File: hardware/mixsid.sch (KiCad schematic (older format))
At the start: 63 parts, among them P1 INPUT, P2 CONTROL, P4 SOCKET LEFT, P5 OUTPUT, P6 SOCKET RIGHT, Q1 BC547, Q2 BC547, U1 GAL16V8, U2 SID2, U3 7812, U4 7809, U5 SID1, U6 4052, U8 ICL7660

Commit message: Project renamed to MixSID
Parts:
- U1: symbol SMARTSID -> MIXSID
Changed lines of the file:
@@
 LIBS:valves
 LIBS:mos6581
-LIBS:smartsid
+LIBS:mixsid
 LIBS:lm78xx
 LIBS:7660
-LIBS:smartsid-cache
+LIBS:mixsid-cache
 EELAYER 25 0
 EELAYER END
@@
 encoding utf-8
 Sheet 1 1
-Title "SmartSID - C64 stereo SID addon board"
+Title "MixSID - C64 stereo SID addon board"
 Date "2016-03-09"
 Rev "1"
 Comp "Henning Bekel"
-Comment1 "www.henning-bekel.de/smartsid"
+Comment1 ""
 Comment2 ""
 Comment3 ""
@@
 $EndComp
 $Comp
-L SMARTSID U1
+L MIXSID U1
 U 1 1 56D81BBF
 P 9300 3450

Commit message: Hardware: Improved routing, placement of 7812 and caps, silkscreen
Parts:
- U3, U4: footprint Power_Integrations:TO-220 -> Pinheaders:TO-220
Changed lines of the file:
@@
 F 0 "U3" H 3550 6804 60  0000 C CNN
 F 1 "7812" H 3400 7200 60  0000 C CNN
-F 2 "Power_Integrations:TO-220" H 3400 7000 60  0001 C CNN
+F 2 "Pinheaders:TO-220" H 3400 7000 60  0001 C CNN
 F 3 "" H 3400 7000 60  0000 C CNN
 	1    3400 7000
@@
 F 0 "U4" H 5300 6804 60  0000 C CNN
 F 1 "7809" H 5150 7200 60  0000 C CNN
-F 2 "Power_Integrations:TO-220" H 5150 7000 60  0001 C CNN
+F 2 "Pinheaders:TO-220" H 5150 7000 60  0001 C CNN
 F 3 "" H 5150 7000 60  0000 C CNN
 	1    5150 7000

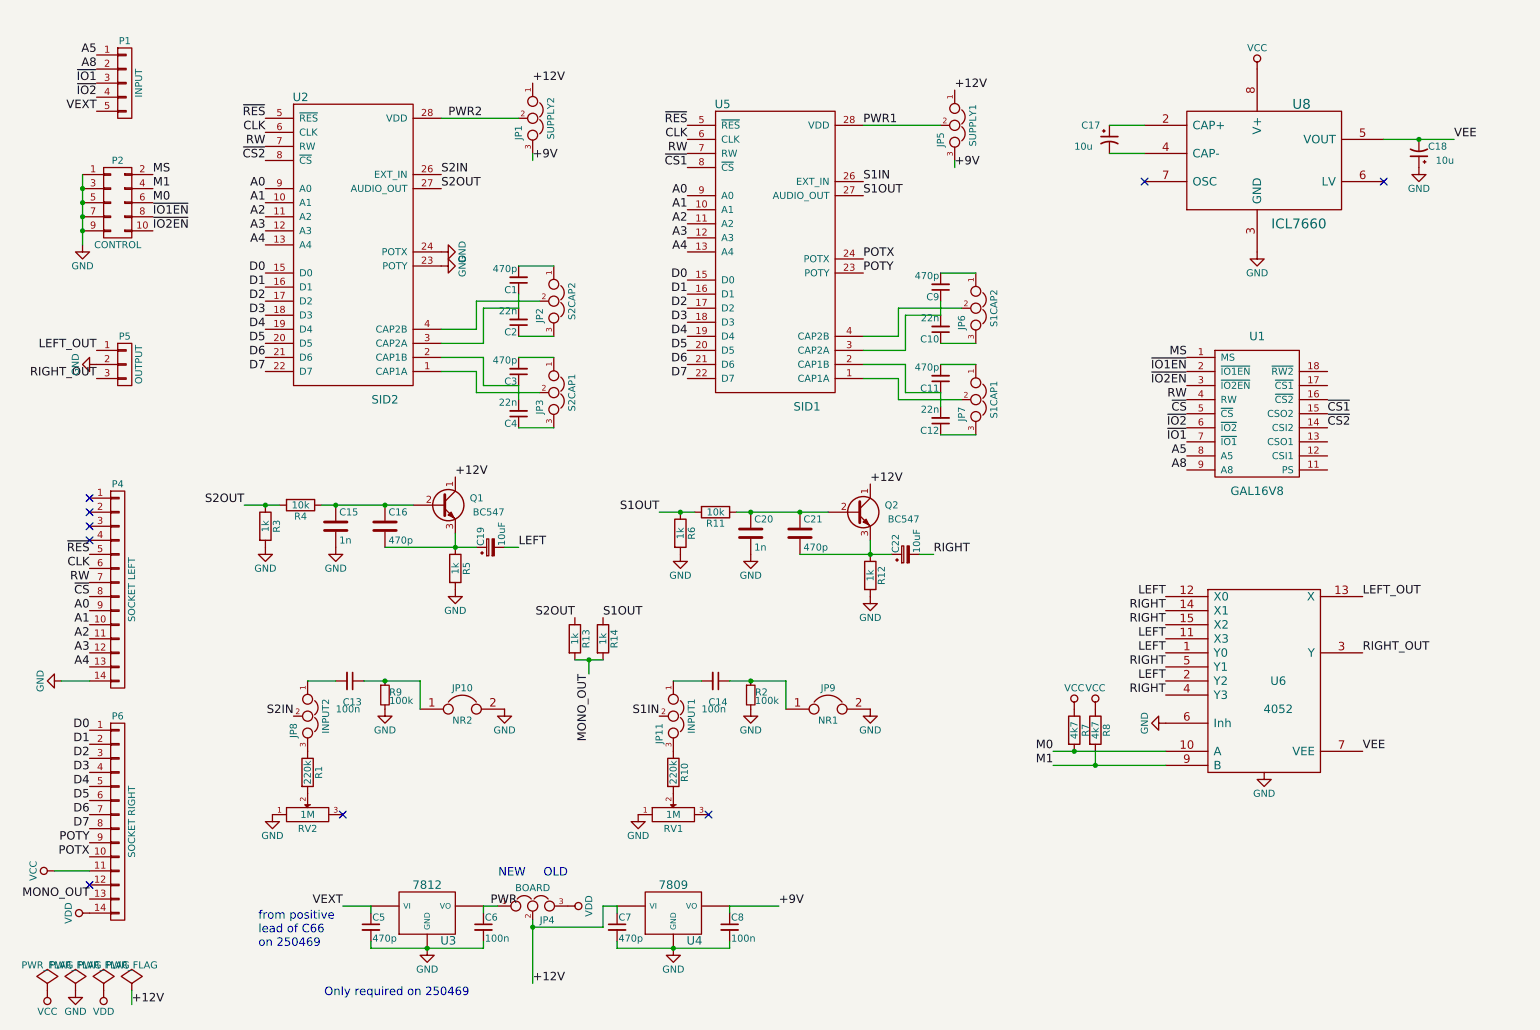
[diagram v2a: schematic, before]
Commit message: Hardware: Added voltage dividers for optional volume adjustments
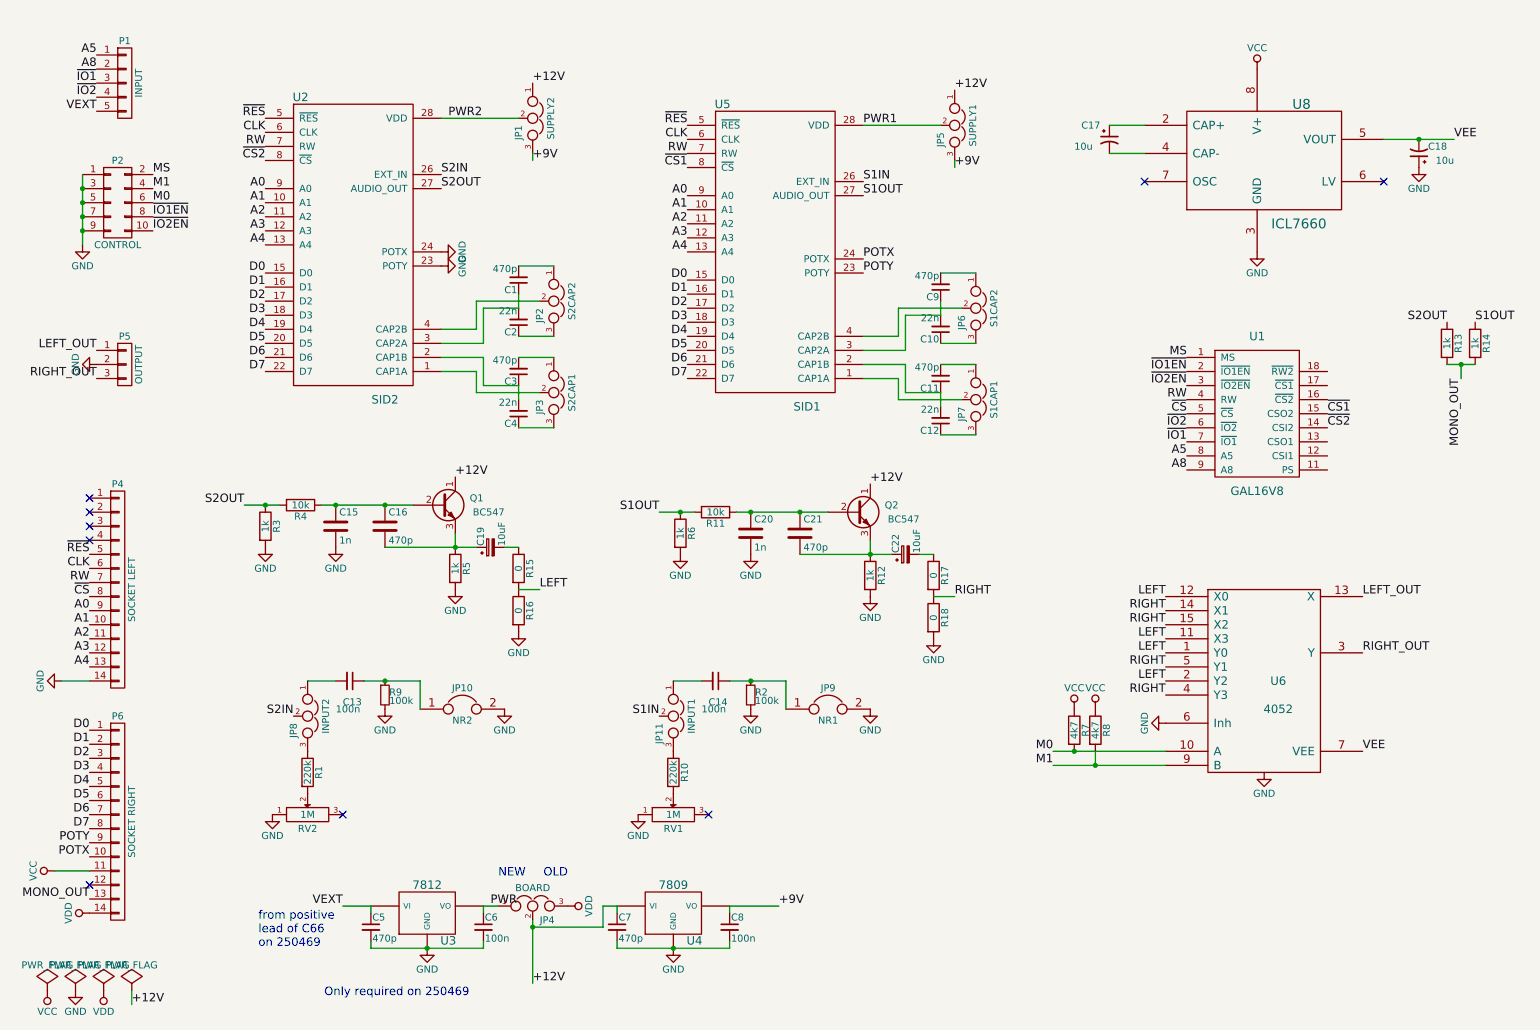
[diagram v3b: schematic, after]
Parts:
- added R15, R16, R17, R18: 0, Discret:R1, symbol R
- C19, C22: footprint Capacitors_ThroughHole:C_Radial_D5_L6_P2.5 -> Pinheaders:C_Radial_D5_L6_P2.5
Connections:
- net GND: now also R16.2, R18.2
- net LEFT: now also R15.2, R16.1; no longer C19.2
- net RIGHT: now also R17.2, R18.1; no longer C22.2
- new net: C19.2, R15.1
- new net: C22.2, R17.1
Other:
- moved on the sheet: R13, R14
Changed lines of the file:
@@
 	0    1    1    0
 $EndComp
-Text Label 7000 4450 0    60   ~ 0
+Text Label 7150 4750 0    60   ~ 0
 RIGHT
-Text Label 4050 4400 0    60   ~ 0
+Text Label 4200 4700 0    60   ~ 0
 LEFT
 $Comp
@@
 Connection ~ 950  2050
 Connection ~ 950  2150
-Text Label 4450 4900 2    60   ~ 0
+Text Label 10650 2800 2    60   ~ 0
 S2OUT
-Text Label 4650 4900 0    60   ~ 0
+Text Label 10850 2800 0    60   ~ 0
 S1OUT
 $Comp
 L R R13
 U 1 1 56EC71A3
-P 4450 5050
-F 0 "R13" V 4530 5050 50  0000 C CNN
-F 1 "1k" V 4450 5050 50  0000 C CNN
-F 2 "Discret:R1" V 4380 5050 50  0001 C CNN
-F 3 "" H 4450 5050 50  0000 C CNN
-	1    4450 5050
+P 10650 2950
+F 0 "R13" V 10730 2950 50  0000 C CNN
+F 1 "1k" V 10650 2950 50  0000 C CNN
+F 2 "Discret:R1" V 10580 2950 50  0001 C CNN
+F 3 "" H 10650 2950 50  0000 C CNN
+	1    10650 2950
 	1    0    0    -1
 $EndComp
@@
 L R R14
 U 1 1 56EC7384
-P 4650 5050
-F 0 "R14" V 4730 5050 50  0000 C CNN
-F 1 "1k" V 4650 5050 50  0000 C CNN
-F 2 "Discret:R1" V 4580 5050 50  0001 C CNN
-F 3 "" H 4650 5050 50  0000 C CNN
-	1    4650 5050
-	1    0    0    -1
-$EndComp
-Wire Wire Line
-	4450 5200 4650 5200
-Wire Wire Line
-	4550 5200 4550 5300
-Connection ~ 4550 5200
-Text Label 4550 5300 3    60   ~ 0
+P 10850 2950
+F 0 "R14" V 10930 2950 50  0000 C CNN
+F 1 "1k" V 10850 2950 50  0000 C CNN
+F 2 "Discret:R1" V 10780 2950 50  0001 C CNN
+F 3 "" H 10850 2950 50  0000 C CNN
+	1    10850 2950
+	1    0    0    -1
+$EndComp
+Wire Wire Line
+	10650 3100 10850 3100
+Wire Wire Line
+	10750 3100 10750 3200
+Connection ~ 10750 3100
+Text Label 10750 3200 3    60   ~ 0
 MONO_OUT
 Text Label 1000 6900 2    60   ~ 0
@@
 F 0 "C19" H 3860 4470 50  0000 L CNN
 F 1 "10uF" H 3860 4320 50  0000 L CNN
-F 2 "Capacitors_ThroughHole:C_Radial_D5_L6_P2.5" H 3850 4400 60  0001 C CNN
+F 2 "Pinheaders:C_Radial_D5_L6_P2.5" H 3850 4400 60  0001 C CNN
 F 3 "" H 3850 4400 60  0000 C CNN
 	1    3850 4400
@@
 F 0 "C22" H 6810 4520 50  0000 L CNN
 F 1 "10uF" H 6810 4370 50  0000 L CNN
-F 2 "Capacitors_ThroughHole:C_Radial_D5_L6_P2.5" H 6800 4450 60  0001 C CNN
+F 2 "Pinheaders:C_Radial_D5_L6_P2.5" H 6800 4450 60  0001 C CNN
 F 3 "" H 6800 4450 60  0000 C CNN
 	1    6800 4450
@@
 	1    0    0    -1
 $EndComp
+$Comp
+L R R15
+U 1 1 571F33A7
+P 4050 4550
+F 0 "R15" V 4130 4550 50  0000 C CNN
+F 1 "0" V 4050 4550 50  0000 C CNN
+F 2 "Discret:R1" V 3980 4550 30  0001 C CNN
+F 3 "" H 4050 4550 30  0000 C CNN
+	1    4050 4550
+	1    0    0    -1
+$EndComp
+$Comp
+L R R16
+U 1 1 571F3464
+P 4050 4850
+F 0 "R16" V 4130 4850 50  0000 C CNN
+F 1 "0" V 4050 4850 50  0000 C CNN
+F 2 "Discret:R1" V 3980 4850 30  0001 C CNN
+F 3 "" H 4050 4850 30  0000 C CNN
+	1    4050 4850
+	1    0    0    -1
+$EndComp
+Wire Wire Line
+	4050 4700 4200 4700
+$Comp
+L GND #PWR037
+U 1 1 571F3E41
+P 4050 5000
+F 0 "#PWR037" H 4050 4750 50  0001 C CNN
+F 1 "GND" H 4050 4850 50  0000 C CNN
+F 2 "" H 4050 5000 60  0000 C CNN
+F 3 "" H 4050 5000 60  0000 C CNN
+	1    4050 5000
+	1    0    0    -1
+$EndComp
+$Comp
+L R R17
+U 1 1 571F4403
+P 7000 4600
+F 0 "R17" V 7080 4600 50  0000 C CNN
+F 1 "0" V 7000 4600 50  0000 C CNN
+F 2 "Discret:R1" V 6930 4600 30  0001 C CNN
+F 3 "" H 7000 4600 30  0000 C CNN
+	1    7000 4600
+	1    0    0    -1
+$EndComp
+$Comp
+L R R18
+U 1 1 571F4409
+P 7000 4900
+F 0 "R18" V 7080 4900 50  0000 C CNN
+F 1 "0" V 7000 4900 50  0000 C CNN
+F 2 "Discret:R1" V 6930 4900 30  0001 C CNN
+F 3 "" H 7000 4900 30  0000 C CNN
+	1    7000 4900
+	1    0    0    -1
+$EndComp
+Wire Wire Line
+	7000 4750 7150 4750
+$Comp
+L GND #PWR038
+U 1 1 571F4410
+P 7000 5050
+F 0 "#PWR038" H 7000 4800 50  0001 C CNN
+F 1 "GND" H 7000 4900 50  0000 C CNN
+F 2 "" H 7000 5050 60  0000 C CNN
+F 3 "" H 7000 5050 60  0000 C CNN
+	1    7000 5050
+	1    0    0    -1
+$EndComp

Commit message: Hardware: Changed 7660 caps to small electrolytics, improved silkscreen
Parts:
- C17, C18: footprint Capacitors_ThroughHole:C_Disc_D3_P2.5 -> Pinheaders:C_Radial_D5_L6_P2.5
- R16, R18: value 0 -> ∞
- U8: footprint Housings_DIP:DIP-8_W7.62mm -> Pinheaders:DIP-8_W7.62mm
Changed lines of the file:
@@
 F 0 "U8" H 9550 2050 70  0000 L CNN
 F 1 "ICL7660" H 9400 1200 70  0000 L CNN
-F 2 "Housings_DIP:DIP-8_W7.62mm" H 9350 1650 60  0001 C CNN
+F 2 "Pinheaders:DIP-8_W7.62mm" H 9350 1650 60  0001 C CNN
 F 3 "" H 9350 1650 60  0000 C CNN
 	1    9350 1650
@@
 F 0 "C17" H 8050 1600 50  0000 L CNN
 F 1 "10u" H 8000 1450 50  0000 L CNN
-F 2 "Capacitors_ThroughHole:C_Disc_D3_P2.5" H 8250 1500 60  0001 C CNN
+F 2 "Pinheaders:C_Radial_D5_L6_P2.5" H 8250 1500 60  0001 C CNN
 F 3 "" H 8250 1500 60  0000 C CNN
 	1    8250 1500
@@
 F 0 "C18" H 10250 1550 50  0000 L CNN
 F 1 "10u" H 10200 1650 50  0000 L CNN
-F 2 "Capacitors_ThroughHole:C_Disc_D3_P2.5" H 10450 1600 60  0001 C CNN
+F 2 "Pinheaders:C_Radial_D5_L6_P2.5" H 10450 1600 60  0001 C CNN
 F 3 "" H 10450 1600 60  0000 C CNN
 	1    10450 1600
@@
 P 4050 4850
 F 0 "R16" V 4130 4850 50  0000 C CNN
-F 1 "0" V 4050 4850 50  0000 C CNN
+F 1 "∞" V 4050 4850 50  0000 C CNN
 F 2 "Discret:R1" V 3980 4850 30  0001 C CNN
 F 3 "" H 4050 4850 30  0000 C CNN
@@
 P 7000 4900
 F 0 "R18" V 7080 4900 50  0000 C CNN
-F 1 "0" V 7000 4900 50  0000 C CNN
+F 1 "∞" V 7000 4900 50  0000 C CNN
 F 2 "Discret:R1" V 6930 4900 30  0001 C CNN
 F 3 "" H 7000 4900 30  0000 C CNN

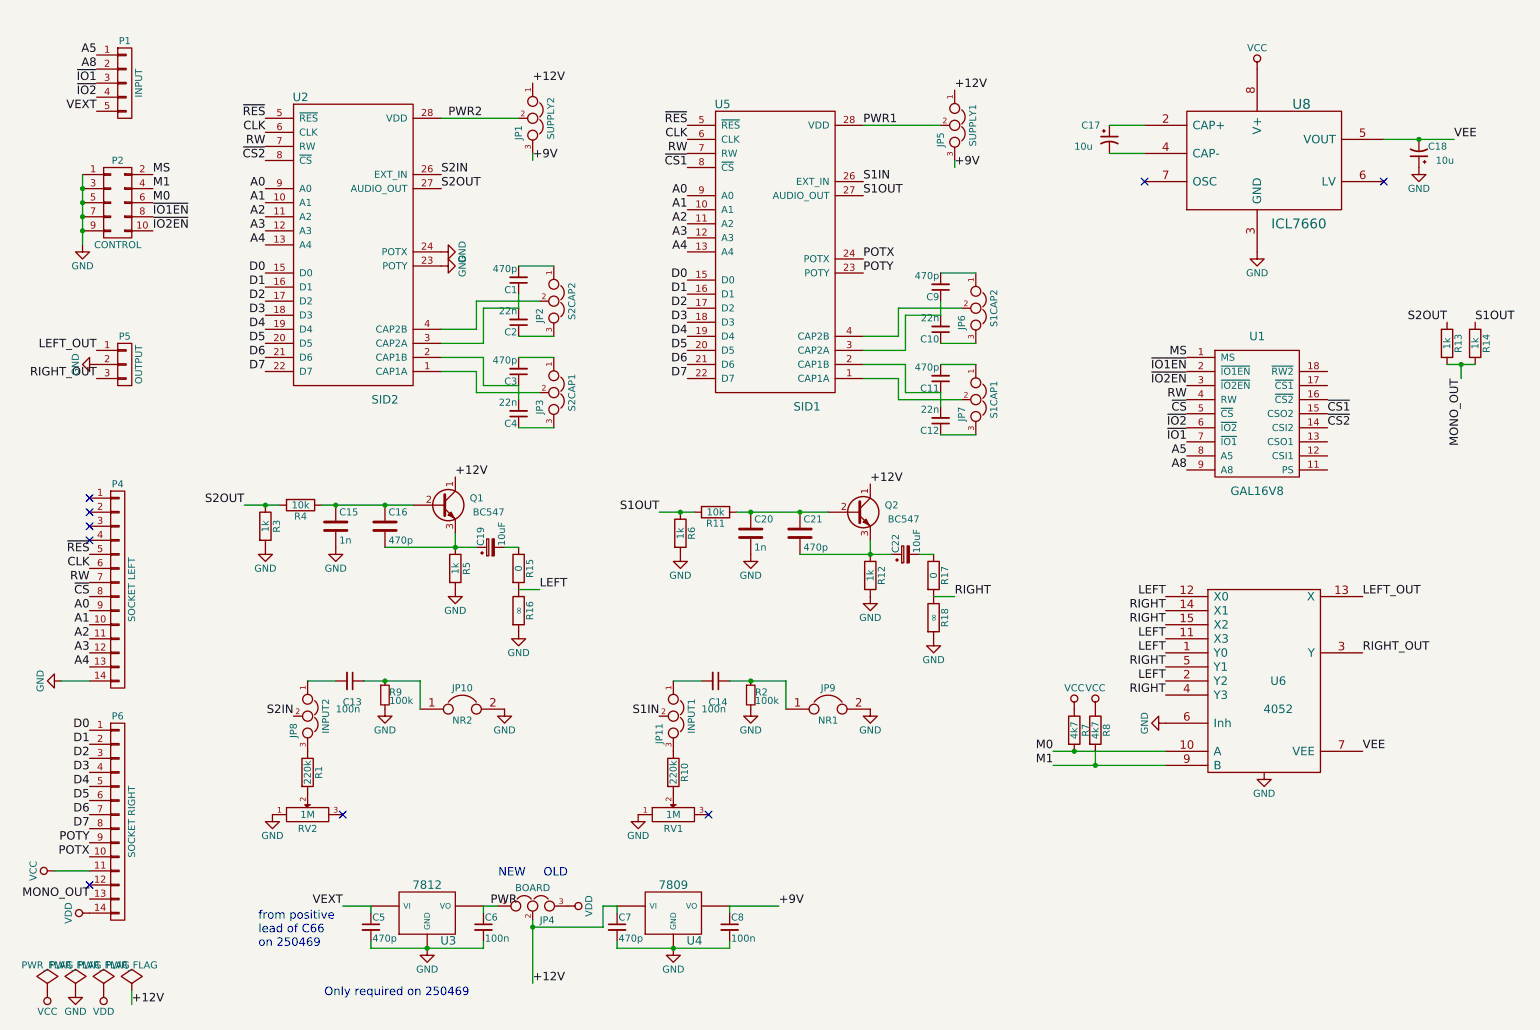
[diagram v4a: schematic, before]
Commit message: Hardware: Priority, paddle multiplexing, volume adjust, bigger board size
Priority select has been reimplemented, allowing to virtually swap sids in
terms of addressing (which SID stays at home and which one goes stereo).

A 4053 multiplexer has been added to keep the paddles working regardless of
priority. Paddle lines are always routed to the SID currently at $d400.

Two pots have been added to allow volume adjustments before mixing in order
to adjust two different models in overall volume (6581 are usually louder).
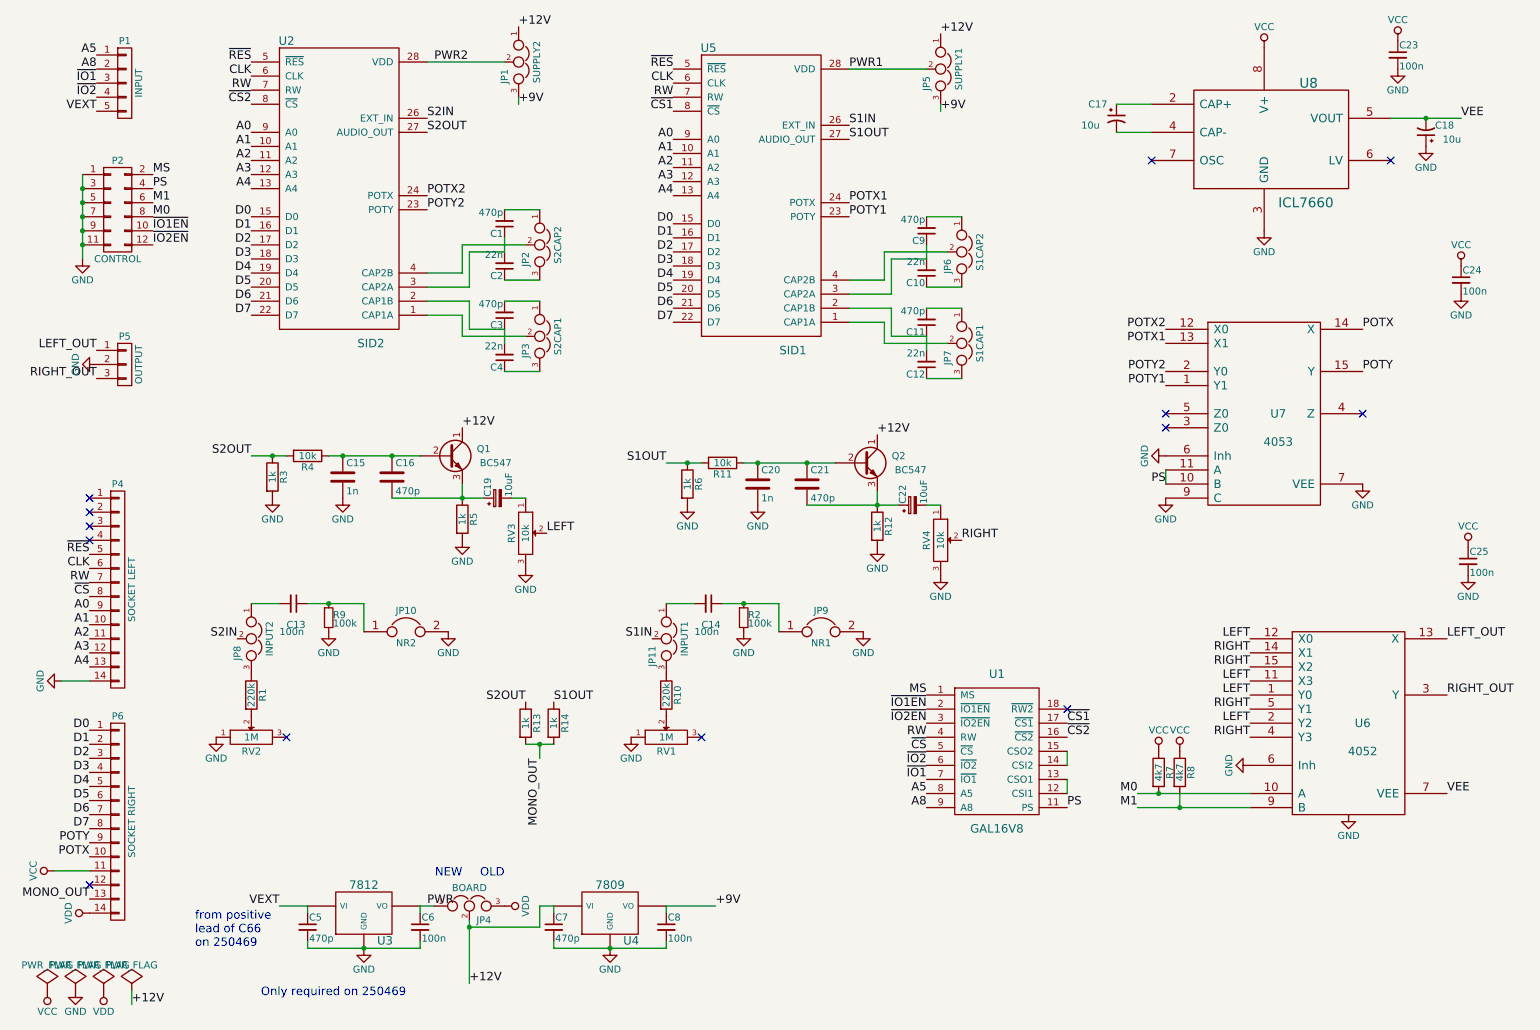
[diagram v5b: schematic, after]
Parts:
- removed P2: CONTROL, Pinheaders:Pin_Header_Straight_2x05, symbol CONN_02X05
- removed R15, R17: 0, Discret:R1, symbol R
- removed R16, R18: ∞, Discret:R1, symbol R
- added C23, C24, C25: 100n, Capacitors_ThroughHole:C_Disc_D3_P2.5, symbol C_Small
- added P2: CONTROL, Pinheaders:Pin_Header_Straight_2x06, symbol CONN_02X06
- added RV3, RV4: 10k, Potentiometers:Potentiometer_Bourns_3296W_3-8Zoll_Inline_ScrewUp, symbol POT
- added U7: 4053, Housings_DIP:DIP-16_W7.62mm, symbol 4053
- R7, R8: footprint Discret:R3 -> Discret:R1
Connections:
- net GND: now also C23.2, C24.2, C25.2, P2.1 (P1), P2.11 (P11), P2.3 (P3), P2.5 (P5), P2.7 (P7), P2.9 (P9), RV3.3, RV4.3, U7.6 (Inh), U7.7 (VEE), U7.8 (GND), U7.9 (C); no longer U2.23 (POTY), U2.24 (POTX)
- net LEFT: now also RV3.2
- net M0: now also P2.8 (P8)
- net M1: now also P2.6 (P6)
- net MS: now also P2.2 (P2)
- net POTX: now also U7.14 (X); no longer U5.24 (POTX)
- net POTY: now also U7.15 (Y); no longer U5.23 (POTY)
- net RIGHT: now also RV4.2
- net VCC: now also C23.1, C24.1, C25.1, U7.16 (VCC)
- net ~CS1: now also U1.17 (~CS1); no longer U1.15 (CSO2)
- net ~CS2: now also U1.16 (~CS2); no longer U1.14 (CSI2)
- net ~IO1EN: now also P2.10 (P10)
- net ~IO2EN: now also P2.12 (P12)
- net PS: now reaches U1.11 (PS)
- net PS: now also P2.4 (P4), U7.10 (B), U7.11 (A)
- net at U1.12 (CSI1): now also U1.13 (CSO1)
- net at C19.2: now also RV3.1
- net at C22.2: now also RV4.1
- new net: U1.14 (CSI2), U1.15 (CSO2)
- new net POTX1: U5.24 (POTX), U7.13 (X1)
- new net POTX2: U2.24 (POTX), U7.12 (X0)
- new net POTY1: U5.23 (POTY), U7.1 (Y1)
- new net POTY2: U2.23 (POTY), U7.2 (Y0)
- no-connect marks 9 -> 13
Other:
- moved on the sheet: C1, C10, C11, C12, C13, C14, C15, C16, C17, C18, C19, C2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
